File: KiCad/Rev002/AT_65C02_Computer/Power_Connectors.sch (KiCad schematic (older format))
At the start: 14 parts, among them J12 Expansion port #2, J14 ESP Interface, J15 Level_Shifter_HV, J16 Level_Shifter_LV, J18 CPU Signals, J19 Address Decoder Enable, J5 Barrel_Jack-Connector, SW1 SW_SPDT, U13 L7806, U6 Regulator_Linear_L7805

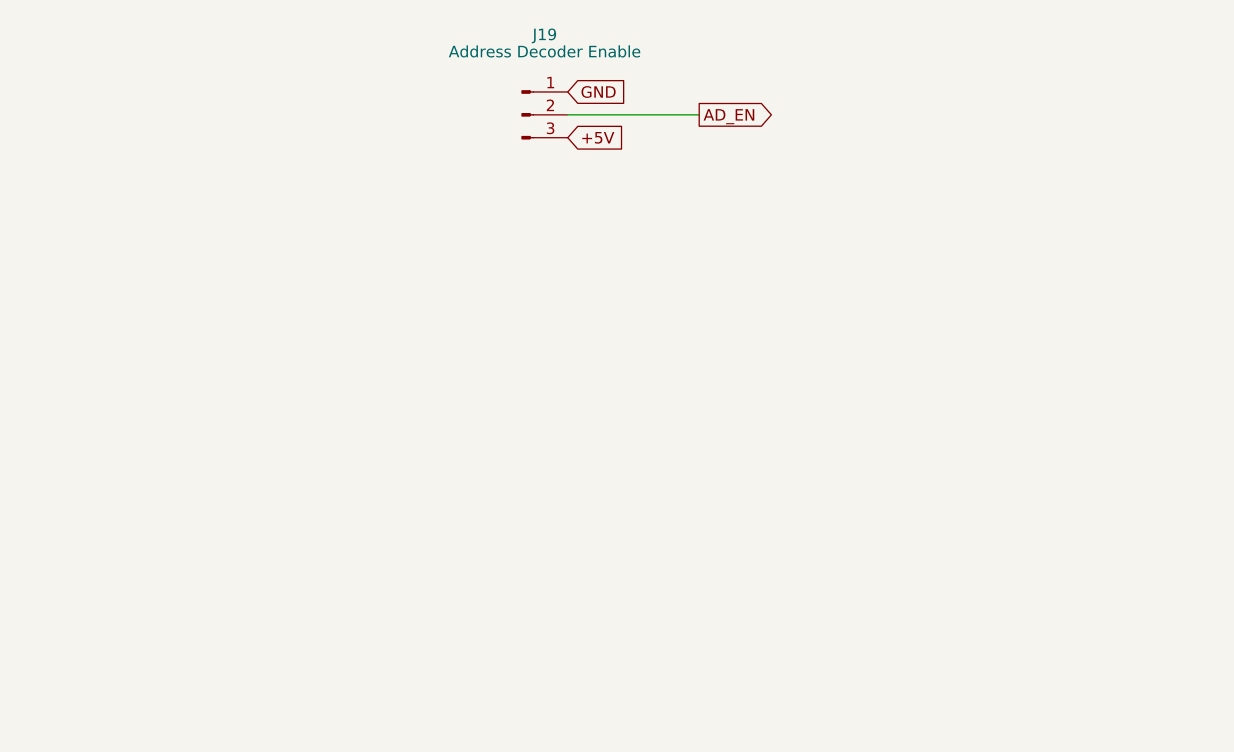
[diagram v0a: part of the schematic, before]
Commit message: HEX Board Mods
Hex board changes. Main board Hex to Latches
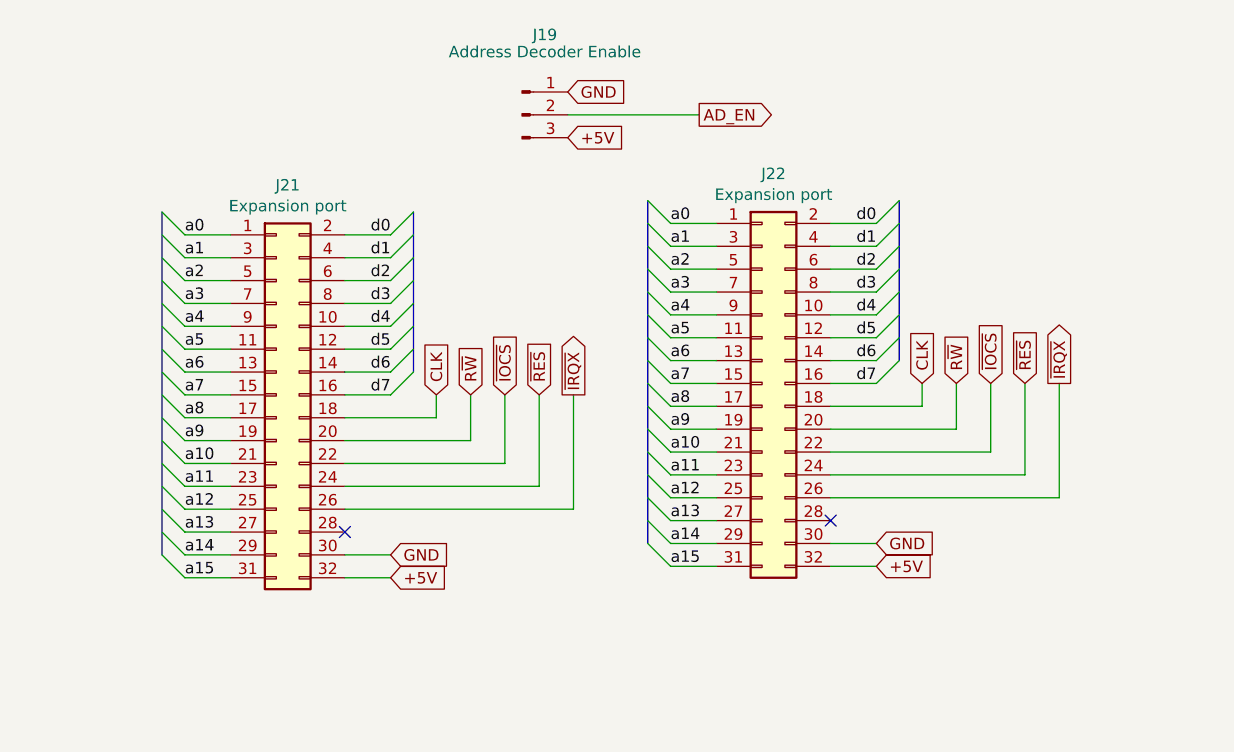
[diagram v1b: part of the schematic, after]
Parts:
- added J21, J22: Expansion port, Connector_PinSocket_2.54mm:PinSocket_2x16_P2.54mm_Vertical, symbol 65C02_Computer-rescue:Conn_02x16_Odd_Even-Connector_Generic
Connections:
- net labels added: CLK, R~W, ~IOCS, ~IRQX, ~RES
- wire segments 59 -> 131
- no-connect marks 9 -> 11

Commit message: release revisions
REv001,002 and HEX
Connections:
- net a0: no longer J12.2 (Pin_2)
- net a1: no longer J12.4 (Pin_4)
- net a10: no longer J12.20 (Pin_20)
- net a11: no longer J12.19 (Pin_19)
- net a12: no longer J12.22 (Pin_22)
- net a13: no longer J12.21 (Pin_21)
- net a14: no longer J12.24 (Pin_24)
- net a15: no longer J12.23 (Pin_23)
- net a2: no longer J12.6 (Pin_6)
- net a3: no longer J12.8 (Pin_8)
- net a4: no longer J12.10 (Pin_10)
- net a5: no longer J12.12 (Pin_12)
- net a6: no longer J12.14 (Pin_14)
- net a7: no longer J12.16 (Pin_16)
- net a8: no longer J12.18 (Pin_18)
- net a9: no longer J12.17 (Pin_17)
- net d0: no longer J12.1 (Pin_1)
- net d1: no longer J12.3 (Pin_3)
- net d2: no longer J12.5 (Pin_5)
- net d3: no longer J12.7 (Pin_7)
- net d4: no longer J12.9 (Pin_9)
- net d5: no longer J12.11 (Pin_11)
- net d6: no longer J12.13 (Pin_13)
- net d7: no longer J12.15 (Pin_15)
- new net ab0: J12.2 (Pin_2)
- new net ab1: J12.4 (Pin_4)
- new net ab10: J12.20 (Pin_20)
- new net ab11: J12.19 (Pin_19)
- new net ab12: J12.22 (Pin_22)
- new net ab13: J12.21 (Pin_21)
- new net ab14: J12.24 (Pin_24)
- new net ab15: J12.23 (Pin_23)
- new net ab2: J12.6 (Pin_6)
- new net ab3: J12.8 (Pin_8)
- new net ab4: J12.10 (Pin_10)
- new net ab5: J12.12 (Pin_12)
- new net ab6: J12.14 (Pin_14)
- new net ab7: J12.16 (Pin_16)
- new net ab8: J12.18 (Pin_18)
- new net ab9: J12.17 (Pin_17)
- new net db0: J12.1 (Pin_1)
- new net db1: J12.3 (Pin_3)
- new net db2: J12.5 (Pin_5)
- new net db3: J12.7 (Pin_7)
- new net db4: J12.9 (Pin_9)
- new net db5: J12.11 (Pin_11)
- new net db6: J12.13 (Pin_13)
- new net db7: J12.15 (Pin_15)
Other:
- moved on the sheet: C10, C31, D1, J15, J16, J18, J19, J21, J22, J5, SW1
